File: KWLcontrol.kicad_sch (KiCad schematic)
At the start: 33 parts, among them J1 Conn_01x03_Pin, J2 Conn_01x03_Socket, J3 Conn_01x03, U1 ESP32-WROOM-32, U2 TPS62172DSG, U3 TPS62172DSG, U4 TXS0101DBV

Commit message: new connectors, some silkscreen
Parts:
- removed J1: Conn_01x03_Pin, Connector_Phoenix_MC:PhoenixContact_MC_1,5_3-GF-3.81_1x03_P3.81mm_Horizontal_ThreadedFlange_MountHole, symbol Connector:Conn_01x03_Pin
- added J4: 2059-323/998-403, KWLcontrol:CONN3_2059-323&slash_998-403_WAG, symbol 2025-02-11_15-19-27:2059-323_998-403
- J2: footprint Connector_Phoenix_MC:PhoenixContact_MCV_1,5_3-G-3.5_1x03_P3.50mm_Vertical -> Connector_Phoenix_MC:PhoenixContact_MC_1,5_3-G-3.81_1x03_P3.81mm_Horizontal
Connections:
- net +12V: now also J2.3 (Pin_3); no longer J2.1 (Pin_1)
- net AC_L: now also J4.5 (3_1), J4.6 (3_2)
- net AC_N: now also J4.3 (2_1), J4.4 (2_2)
- net AC_PE: now also J4.1 (1_1), J4.2 (1_2)
- net GNDREF: now also J2.1 (Pin_1); no longer J2.3 (Pin_3)
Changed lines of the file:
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@@
 	(paper "A4")
 	(junction
+		(at 36.83 50.8)
+		(diameter 0)
+		(color 0 0 0 0)
+	)
+	(junction
 		(at 171.45 87.63)
 		(diameter 0)
@@
 	)
 	(junction
+		(at 36.83 55.88)
+		(diameter 0)
+		(color 0 0 0 0)
+	)
+	(junction
 		(at 38.1 76.2)
 		(diameter 0)
@@
 	)
 	(junction
+		(at 36.83 45.72)
+		(diameter 0)
+		(color 0 0 0 0)
+	)
+	(junction
 		(at 63.5 118.11)
 		(diameter 0)
@@
 	(wire
 		(pts
+			(xy 33.02 50.8) (xy 36.83 50.8)
+		)
+		(stroke
+			(width 0)
+			(type default)
+		)
+	)
+	(wire
+		(pts
 			(xy 232.41 31.75) (xy 243.84 31.75)
 		)
@@
 	(wire
 		(pts
-			(xy 38.1 53.34) (xy 43.18 53.34)
+			(xy 33.02 53.34) (xy 36.83 53.34)
 		)
 		(stroke
@@
 	(wire
 		(pts
+			(xy 36.83 55.88) (xy 77.47 55.88)
+		)
+		(stroke
+			(width 0)
+			(type default)
+		)
+	)
+	(wire
+		(pts
 			(xy 86.36 120.65) (xy 99.06 120.65)
 		)
@@
 	(wire
 		(pts
-			(xy 43.18 53.34) (xy 43.18 55.88)
+			(xy 88.9 118.11) (xy 86.36 118.11)
 		)
 		(stroke
@@
 	(wire
 		(pts
-			(xy 88.9 118.11) (xy 86.36 118.11)
+			(xy 240.03 95.25) (xy 234.95 95.25)
 		)
 		(stroke
@@
 	(wire
 		(pts
-			(xy 43.18 45.72) (xy 67.31 45.72)
+			(xy 167.64 87.63) (xy 171.45 87.63)
 		)
 		(stroke
@@
 	(wire
 		(pts
-			(xy 240.03 95.25) (xy 234.95 95.25)
+			(xy 240.03 99.06) (xy 240.03 95.25)
 		)
 		(stroke
@@
 	(wire
 		(pts
-			(xy 167.64 87.63) (xy 171.45 87.63)
+			(xy 242.57 130.81) (xy 234.95 130.81)
 		)
 		(stroke
@@
 	(wire
 		(pts
-			(xy 240.03 99.06) (xy 240.03 95.25)
+			(xy 194.31 87.63) (xy 190.5 87.63)
 		)
 		(stroke
@@
 	(wire
 		(pts
-			(xy 242.57 130.81) (xy 234.95 130.81)
+			(xy 33.02 55.88) (xy 36.83 55.88)
 		)
 		(stroke
@@
 	(wire
 		(pts
-			(xy 194.31 87.63) (xy 190.5 87.63)
+			(xy 171.45 87.63) (xy 180.34 87.63)
 		)
 		(stroke
@@
 	(wire
 		(pts
-			(xy 171.45 87.63) (xy 180.34 87.63)
+			(xy 76.2 95.25) (xy 78.74 95.25)
 		)
 		(stroke
@@
 	(wire
 		(pts
-			(xy 76.2 95.25) (xy 78.74 95.25)
+			(xy 36.83 58.42) (xy 36.83 55.88)
 		)
 		(stroke
@@
 	(wire
 		(pts
-			(xy 38.1 50.8) (xy 67.31 50.8)
-		)
-		(stroke
-			(width 0)
-			(type default)
-		)
-	)
-	(wire
-		(pts
 			(xy 46.99 118.11) (xy 63.5 118.11)
 		)
@@
 	(wire
 		(pts
-			(xy 43.18 55.88) (xy 77.47 55.88)
+			(xy 78.74 99.06) (xy 78.74 95.25)
 		)
 		(stroke
@@
 	(wire
 		(pts
-			(xy 78.74 99.06) (xy 78.74 95.25)
+			(xy 36.83 50.8) (xy 67.31 50.8)
 		)
 		(stroke
@@
 	(wire
 		(pts
-			(xy 63.5 128.27) (xy 66.04 128.27)
+			(xy 33.02 58.42) (xy 36.83 58.42)
 		)
 		(stroke
@@
 	(wire
 		(pts
-			(xy 43.18 45.72) (xy 43.18 48.26)
+			(xy 63.5 128.27) (xy 66.04 128.27)
 		)
 		(stroke
@@
 	(wire
 		(pts
+			(xy 33.02 48.26) (xy 36.83 48.26)
+		)
+		(stroke
+			(width 0)
+			(type default)
+		)
+	)
+	(wire
+		(pts
 			(xy 87.63 45.72) (xy 101.6 45.72)
 		)
@@
 	(wire
 		(pts
+			(xy 36.83 53.34) (xy 36.83 50.8)
+		)
+		(stroke
+			(width 0)
+			(type default)
+		)
+	)
+	(wire
+		(pts
+			(xy 36.83 48.26) (xy 36.83 45.72)
+		)
+		(stroke
+			(width 0)
+			(type default)
+		)
+	)
+	(wire
+		(pts
 			(xy 104.14 118.11) (xy 113.03 118.11)
 		)
@@
 	(wire
 		(pts
+			(xy 36.83 45.72) (xy 67.31 45.72)
+		)
+		(stroke
+			(width 0)
+			(type default)
+		)
+	)
+	(wire
+		(pts
 			(xy 48.26 76.2) (xy 63.5 76.2)
 		)
@@
 	(wire
 		(pts
-			(xy 43.18 48.26) (xy 38.1 48.26)
+			(xy 33.02 45.72) (xy 36.83 45.72)
 		)
 		(stroke
@@
 	)
 	(symbol
+		(lib_id "2025-02-11_15-19-27:2059-323_998-403")
+		(at 33.02 58.42 180)
+		(unit 1)
+		(exclude_from_sim no)
+		(in_bom yes)
+		(on_board yes)
+		(dnp no)
+		(fields_autoplaced yes)
+		(property "Reference" "J4"
+			(at 24.13 38.1 0)
+			(effects
+				(font
+					(size 1.524 1.524)
+				)
+			)
+		)
+		(property "Value" "2059-323/998-403"
+			(at 24.13 40.64 0)
+			(effects
+				(font
+					(size 1.524 1.524)
+				)
+			)
+		)
+		(property "Footprint" "KWLcontrol:CONN3_2059-323&slash_998-403_WAG"
+			(at 33.02 58.42 0)
+			(effects
+				(font
+					(size 1.27 1.27)
+					(italic yes)
+				)
+				(hide yes)
+			)
+		)
+		(property "Datasheet" "2059-323/998-403"
+			(at 33.02 58.42 0)
+			(effects
+				(font
+					(size 1.27 1.27)
+					(italic yes)
+				)
+				(hide yes)
+			)
+		)
+		(property "Description" ""
+			(at 33.02 58.42 0)
+			(effects
+				(font
+					(size 1.27 1.27)
+				)
+				(hide yes)
+			)
+		)
+		(pin "4"
+		)
+		(pin "3"
+		)
+		(pin "6"
+		)
+		(pin "1"
+		)
+		(pin "5"
+		)
+		(pin "2"
+		)
+		(instances
+			(project ""
+				(path "/4fb2b777-e625-4fb4-a25a-05d46bd9d657"
+					(reference "J4")
+					(unit 1)
+				)
+			)
+		)
+	)
+	(symbol
 		(lib_id "power:+5V")
 		(at 53.34 86.36 0)
@@
 	)
 	(symbol
-		(lib_id "Connector:Conn_01x03_Pin")
-		(at 33.02 50.8 0)
-		(unit 1)
-		(exclude_from_sim no)
-		(in_bom yes)
-		(on_board yes)
-		(dnp no)
-		(fields_autoplaced yes)
-		(property "Reference" "J1"
-			(at 33.655 43.18 0)
-			(effects
-				(font
-					(size 1.27 1.27)
-				)
-			)
-		)
-		(property "Value" "Conn_01x03_Pin"
-			(at 33.655 45.72 0)
-			(effects
-				(font
-					(size 1.27 1.27)
-				)
-			)
-		)
-		(property "Footprint" "Connector_Phoenix_MC:PhoenixContact_MC_1,5_3-GF-3.81_1x03_P3.81mm_Horizontal_ThreadedFlange_MountHole"
-			(at 33.02 50.8 0)
-			(effects
-				(font
-					(size 1.27 1.27)
-				)
-				(hide yes)
-			)
-		)
-		(property "Datasheet" "~"
-			(at 33.02 50.8 0)
-			(effects
-				(font
-					(size 1.27 1.27)
-				)
-				(hide yes)
-			)
-		)
-		(property "Description" "Generic connector, single row, 01x03, script generated"
-			(at 33.02 50.8 0)
-			(effects
-				(font
-					(size 1.27 1.27)
-				)
-				(hide yes)
-			)
-		)
-		(pin "3"
-		)
-		(pin "2"
-		)
-		(pin "1"
-		)
-		(instances
-			(project ""
-				(path "/4fb2b777-e625-4fb4-a25a-05d46bd9d657"
-					(reference "J1")
-					(unit 1)
-				)
-			)
-		)
-	)
-	(symbol
 		(lib_id "power:GNDREF")
 		(at 260.35 87.63 90)
@@
 		(lib_id "Connector:Conn_01x03_Socket")
 		(at 248.92 34.29 0)
+		(mirror x)
 		(unit 1)
 		(exclude_from_sim no)
@@
 		(on_board yes)
 		(dnp no)
-		(fields_autoplaced yes)
 		(property "Reference" "J2"
-			(at 250.19 33.0199 0)
+			(at 250.19 35.5601 0)
 			(effects
 				(font
@@
 		)
 		(property "Value" "Conn_01x03_Socket"
-			(at 250.19 35.5599 0)
+			(at 250.19 33.0201 0)
 			(effects
 				(font
@@
 			)
 		)
-		(property "Footprint" "Connector_Phoenix_MC:PhoenixContact_MCV_1,5_3-G-3.5_1x03_P3.50mm_Vertical"
+		(property "Footprint" "Connector_Phoenix_MC:PhoenixContact_MC_1,5_3-G-3.81_1x03_P3.81mm_Horizontal"
 			(at 248.92 34.29 0)
 			(effects

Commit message: minor changes and improvements
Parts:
- added R9: 1M, Resistor_SMD:R_0805_2012Metric_Pad1.20x1.40mm_HandSolder, symbol Device:R
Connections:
- net +3.3V: no longer C3.1
- net AC_PE: now also PS1.10 (NC), PS1.11 (NC), PS1.12 (NC), PS1.13 (NC), R9.2
- net GNDREF: now also PS1.15 (NC), PS1.17 (NC), PS1.22 (NC), PS1.24 (NC), PS1.26 (NC), R9.1
- net at R4.2, U1.3 (EN): now also C3.1
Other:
- moved on the sheet: C3, R4

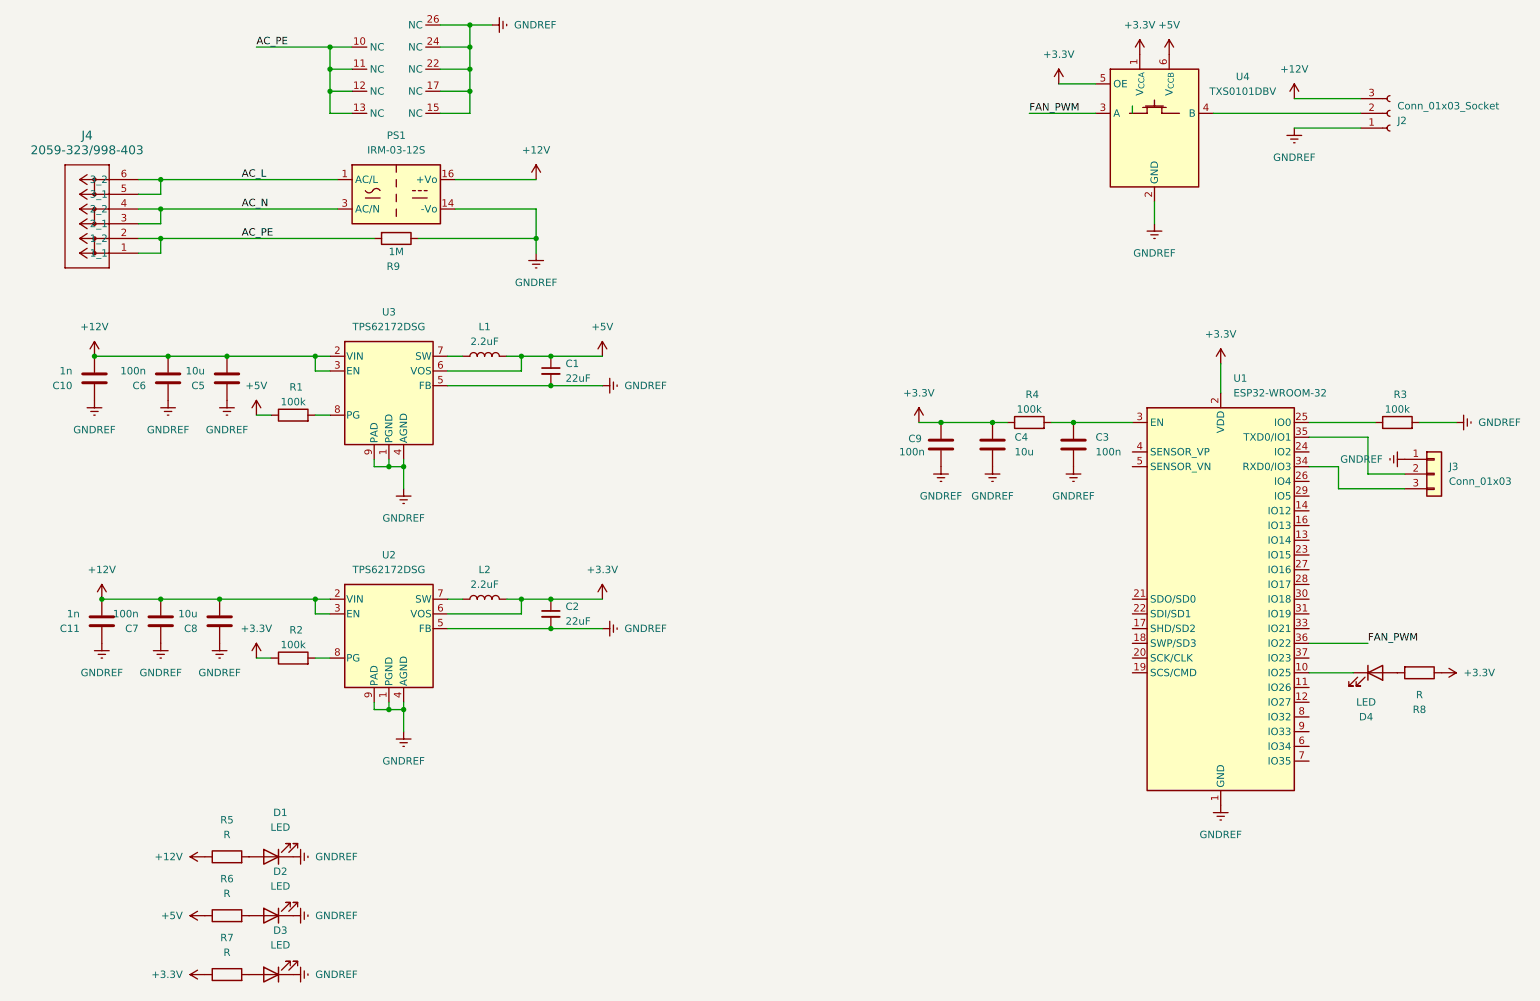
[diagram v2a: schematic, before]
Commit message: improvements, add BME680
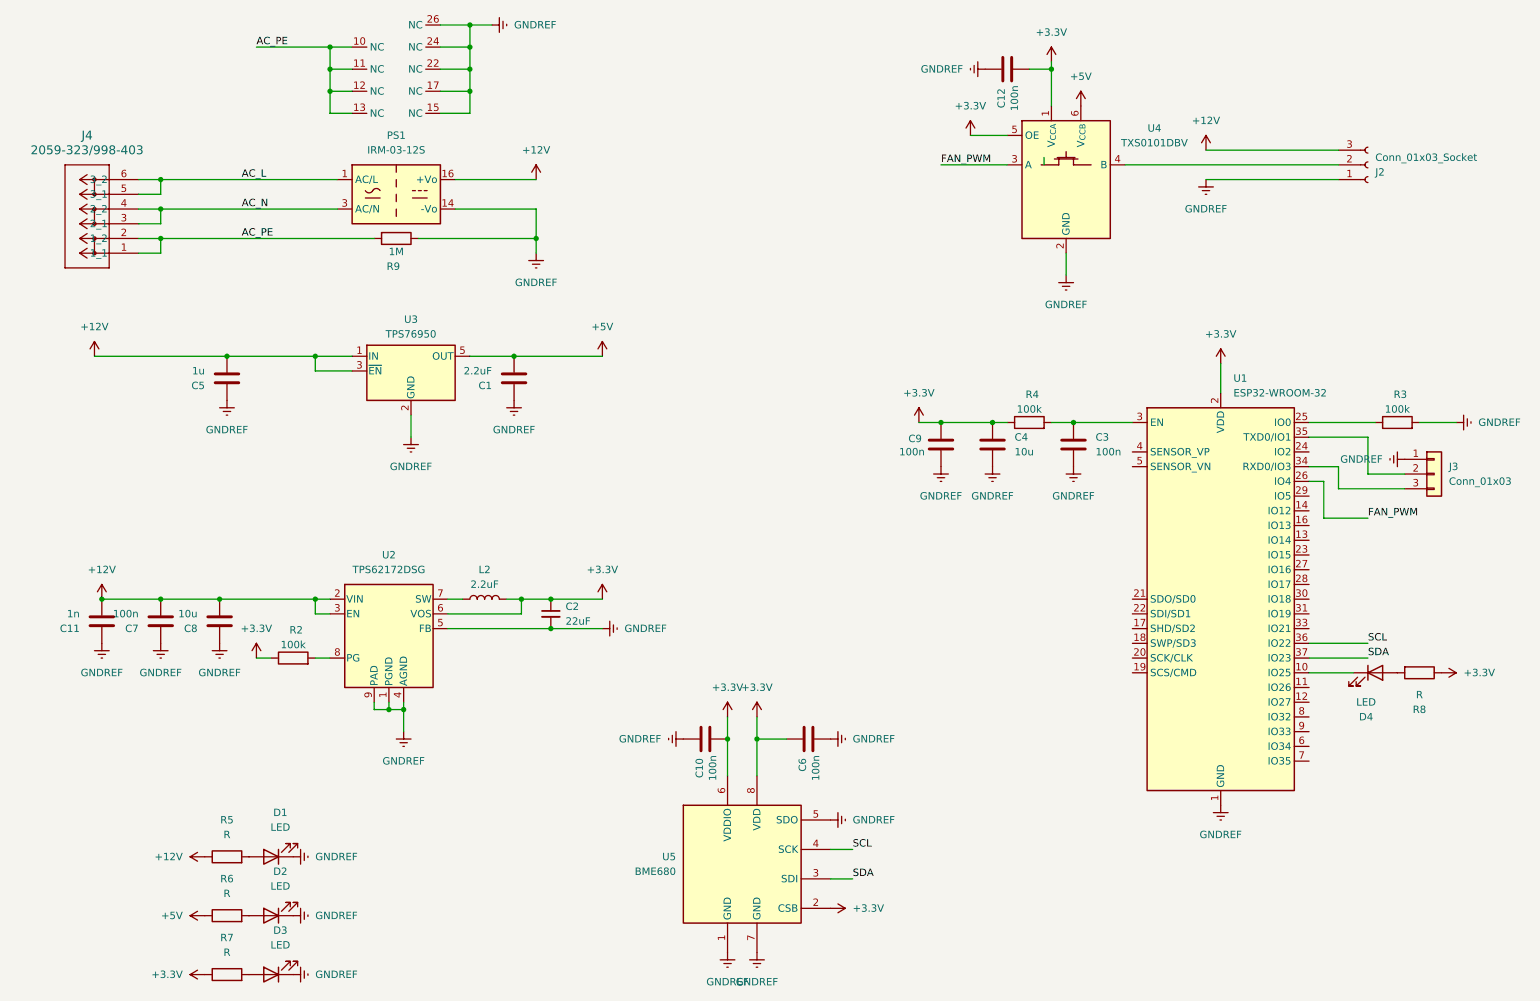
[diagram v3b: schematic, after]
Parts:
- removed C1: 22uF, Capacitor_SMD:C_0805_2012Metric_Pad1.18x1.45mm_HandSolder, symbol Device:C_Small
- removed L1: 2.2uF, Inductor_SMD:L_0805_2012Metric_Pad1.15x1.40mm_HandSolder, symbol Device:L
- removed R1: 100k, Resistor_SMD:R_0805_2012Metric_Pad1.20x1.40mm_HandSolder, symbol Device:R
- removed U3: TPS62172DSG, Package_SON:WSON-8-1EP_2x2mm_P0.5mm_EP0.9x1.6mm_ThermalVias, symbol Regulator_Switching:TPS62172DSG
- added C1: 2.2uF, Capacitor_SMD:C_0805_2012Metric_Pad1.18x1.45mm_HandSolder, symbol Device:C
- added C12: 100n, Capacitor_SMD:C_0805_2012Metric_Pad1.18x1.45mm_HandSolder, symbol Device:C
- added U3: TPS76950, Package_TO_SOT_SMD:SOT-23-5, symbol Regulator_Linear:TPS76950
- added U5: BME680, Package_LGA:Bosch_LGA-8_3x3mm_P0.8mm_ClockwisePinNumbering, symbol Sensor:BME680
- C10: value 1n -> 100n
- C5: value 10u -> 1u
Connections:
- net +12V: now also U3.1 (IN), U3.3 (~{EN}); no longer C10.2, C6.2
- net +3.3V: now also C10.1, C6.2, C12.1, U5.2 (CSB), U5.6 (VDDIO), U5.8 (VDD)
- net +5V: now also C1.2, U3.5 (OUT)
- net FAN_PWM: now also U1.26 (IO4); no longer U1.36 (IO22)
- net GNDREF: now also C10.2, C1.1, C12.2, U3.2 (GND), U5.1 (GND), U5.5 (SDO), U5.7 (GND); no longer C10.1
- net SDA: now reaches U1.37 (IO23)
- net SDA: now also U5.3 (SDI)
- new net SCL: U1.36 (IO22), U5.4 (SCK)
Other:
- moved on the sheet: J2, U4
